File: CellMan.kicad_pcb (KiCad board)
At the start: 2 copper layers, 99.4 x 45 mm, 74 parts, among them J1 Conn_01x04_Male, J2 Conn_01x04_Male, J3 Conn_01x04_Male, J4 Conn_01x02_Female, J5 Conn_01x03_Male, Q1 BSS138W, Q2 STS8DN6LF6AG, Q3 BSS138W, Q4 BSS138W, Q5 BSS138W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

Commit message: something minor
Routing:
- net /SafeGND: track 36.2 -> 62.9 mm, vias 14 -> 17
- net /Balancing: track 3.73 -> 18.0 mm
- net +3V3: track 194.0 -> 192.9 mm

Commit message: zero unrouted traces baby
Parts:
- C4: moved to B.Cu
- moved D4 78.0 mm to (107.5, 118.5), turned to 180 degrees
- moved R21 74.4 mm to (111.3, 118.5), turned to 180 degrees
- moved R19 57.4 mm to (120.7, 117.9), turned to 90 degrees
- moved Q4 56.4 mm to (124.8, 117.8), turned to 180 degrees
- moved C4 13.0 mm to (163.8, 96.7), turned to 180 degrees
- moved C3 9.07 mm to (159.7, 92.9), turned to 270 degrees
- moved U2 5.25 mm to (170.7, 93.1), turned to 180 degrees
- moved C2 1.65 mm to (176.9, 88.0), turned to 90 degrees
- moved U1 0.12 mm to (150.4, 87.9)
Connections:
- ISO2 pad 4: /voltage_measurement/SafeCell- -> /SafeCell-
- U1 pad 16: /Balance_ctl -> Net-(U1-Pad16)
- U1 pad 17: /IO_Sanity_Check -> Net-(U1-Pad17)
- U1 pad 18: +3V3 -> /Balance_ctl
- U1 pad 19: (no net) -> /IO_Sanity_Check
- U1 pad 20: (no net) -> +3V3
- U9 pad 2: /voltage_measurement/SafeCell- -> /SafeCell-
- U9 pad 4: /voltage_measurement/SafeCell- -> /SafeCell-
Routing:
- net /Address_T0: track 2.77 -> 52.8 mm, vias 1 -> 3
- net /Address_T1: track 2.58 -> 52.4 mm, vias 1 -> 3
- net /Address_T2: track 2.25 -> 51.9 mm, vias 1 -> 3
- net /SafeGND: track 62.9 -> 92.0 mm, vias 17 -> 22
- net /Cell+: track 140.5 -> 168.0 mm, vias 2 -> 6
- net +3V3: track 192.9 -> 206.6 mm, vias 13 -> 16
- net /Cell-: track 126.6 -> 138.5 mm, vias 5 -> 3
- net /SCL: track 90.4 -> 98.3 mm, vias 3 -> 4
- net /SDA: track 82.3 -> 88.5 mm, vias 3 -> 4
- net /SafeCell-: track 0.00 -> 5.41 mm, vias 0 -> 3
- net /Balancing: track 18.0 -> 20.8 mm, vias 1 -> 2
- net GND: track 86.2 -> 88.9 mm, vias 4 -> 5
- net /voltage_measurement/SafeCell-: track 2.59 -> 0.00 mm
- net Net-(D4-Pad1): track 0.00 -> 1.84 mm
- net /Balance_ctl: track 32.1 -> 32.2 mm, vias 0 -> 2
- added copper zone on B.Cu, net /SafeCell-

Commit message: memes
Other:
- board text added: "+"
- board text added: "-"
- board text added: "Address Select"
- board text added: "Connor Winiarczyk"
- board text added: "Is this text rules compliant?"
- board text added: "WARNING DO NOT LICK!"
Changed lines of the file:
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@@
   (general
     (thickness 1.6)
-    (drawings 4)
+    (drawings 12)
     (tracks 638)
     (zones 0)
@@
   )
   (setup
-    (last_trace_width 0.25)
+    (last_trace_width 1.5)
     (user_trace_width 1.5)
     (trace_clearance 0.2)
@@
     (tags "resistor handsolder")
     (attr smd)
-    (fp_text reference R19 (at -3.4 0 90) (layer F.SilkS)
+    (fp_text reference R19 (at 3.375 0.025 90) (layer F.SilkS)
       (effects (font (size 1 1) (thickness 0.15)))
     )
@@
     (tags "SOT-323 SC-70 Handsoldering")
     (attr smd)
-    (fp_text reference Q4 (at 0 -2) (layer F.SilkS)
+    (fp_text reference Q4 (at 0 2.375) (layer F.SilkS)
       (effects (font (size 1 1) (thickness 0.15)))
     )
@@
     (descr "Through hole angled pin header, 1x03, 2.54mm pitch, 6mm pin length, single row")
     (tags "Through hole angled pin header THT 1x03 2.54mm single row")
-    (fp_text reference J5 (at 4.385 -2.27) (layer F.SilkS)
+    (fp_text reference J5 (at -2.45 -0.1) (layer F.SilkS)
       (effects (font (size 1 1) (thickness 0.15)))
     )
@@
     (tags "mounting hole 4.5mm")
     (attr virtual)
-    (fp_text reference H7 (at 0 -5.5) (layer F.SilkS)
+    (fp_text reference H7 (at -4.13 -4.96) (layer F.SilkS)
       (effects (font (size 1 1) (thickness 0.15)))
     )
@@
     (tags "mounting hole 4.5mm")
     (attr virtual)
-    (fp_text reference H6 (at 0 -5.5) (layer F.SilkS)
+    (fp_text reference H6 (at -3.575 -4.71) (layer F.SilkS)
       (effects (font (size 1 1) (thickness 0.15)))
     )
@@
     (tags "mounting hole 4.5mm")
     (attr virtual)
-    (fp_text reference H5 (at 0 -5.5) (layer F.SilkS)
+    (fp_text reference H5 (at 3.115 -4.76) (layer F.SilkS)
       (effects (font (size 1 1) (thickness 0.15)))
     )
@@
     (tags "mounting hole 4.5mm")
     (attr virtual)
-    (fp_text reference H4 (at 0 -5.5) (layer F.SilkS)
+    (fp_text reference H4 (at 4.035 -4.15) (layer F.SilkS)
       (effects (font (size 1 1) (thickness 0.15)))
     )
@@
     (tags "mounting hole 4.5mm")
     (attr virtual)
-    (fp_text reference H3 (at 0 -5.5) (layer F.SilkS)
+    (fp_text reference H3 (at 3.185 -4.985) (layer F.SilkS)
       (effects (font (size 1 1) (thickness 0.15)))
     )
@@
     (tags "mounting hole 4.5mm")
     (attr virtual)
-    (fp_text reference H2 (at 0 -5.5) (layer F.SilkS)
+    (fp_text reference H2 (at -2.3 -5.175) (layer F.SilkS)
       (effects (font (size 1 1) (thickness 0.15)))
     )
@@
     (tags "mounting hole 4.5mm")
     (attr virtual)
-    (fp_text reference H1 (at 0 -5.5) (layer F.SilkS)
+    (fp_text reference H1 (at 2.915 -4.9) (layer F.SilkS)
       (effects (font (size 1 1) (thickness 0.15)))
     )
@@
     (descr "8-lead though-hole mounted DIP package, row spacing 7.62 mm (300 mils)")
     (tags "THT DIP DIL PDIP 2.54mm 7.62mm 300mil")
-    (fp_text reference ISO2 (at 3.81 -2.33 90) (layer F.SilkS)
+    (fp_text reference ISO2 (at 3.8753 9.8528 90) (layer F.SilkS)
       (effects (font (size 1 1) (thickness 0.15)))
     )
@@
     (descr "Through hole angled pin header, 1x04, 2.54mm pitch, 6mm pin length, single row")
     (tags "Through hole angled pin header THT 1x04 2.54mm single row")
-    (fp_text reference J1 (at 4.385 -2.27) (layer F.SilkS)
+    (fp_text reference J1 (at -3.45 6.625) (layer F.SilkS)
       (effects (font (size 1 1) (thickness 0.15)))
     )
@@
     (tags "resistor handsolder")
     (attr smd)
-    (fp_text reference R14 (at 0 -1.65 90) (layer F.SilkS)
+    (fp_text reference R14 (at 3.3 0.025 90) (layer F.SilkS)
       (effects (font (size 1 1) (thickness 0.15)))
     )
@@
     )
   )
+  (gr_text "WARNING\nDO NOT LICK!" (at 135.175 107.1) (layer B.SilkS)
+    (effects (font (size 1 1) (thickness 0.15)) (justify mirror))
+  )
+  (gr_text - (at 178.45 105.15 180) (layer F.SilkS)
+    (effects (font (size 4 4) (thickness 0.5)) (justify left))
+  )
+  (gr_text + (at 106.775 107.675 90) (layer F.SilkS)
+    (effects (font (size 4 4) (thickness 0.5)) (justify left))
+  )
+  (gr_text "Address Select" (at 127.85 109.75 90) (layer F.SilkS)
+    (effects (font (size 1 1) (thickness 0.15)) (justify left))
+  )
+  (gr_text "Connor\nWiniarczyk" (at 183.1 120.9) (layer F.Mask)
+    (effects (font (size 1.5 1.5) (thickness 0.3)))
+  )
+  (gr_text "Connor\nWiniarczyk" (at 183.1 120.9) (layer F.Cu)
+    (effects (font (size 1.5 1.5) (thickness 0.3)))
+  )
+  (gr_text "Is this\ntext rules \ncompliant?" (at 117.357143 120.95) (layer B.Mask)
+    (effects (font (size 1.5 1.5) (thickness 0.3)) (justify left mirror))
+  )
+  (gr_text "Is this\ntext rules \ncompliant?" (at 117.357143 120.95) (layer B.Cu)
+    (effects (font (size 1.5 1.5) (thickness 0.3)) (justify left mirror))
+  )
   (gr_line (start 191.08 82.38) (end 191.08 127.38) (layer Edge.Cuts) (width 0.05))
   (gr_line (start 91.66 82.38) (end 191.08 82.38) (layer Edge.Cuts) (width 0.05))
   (gr_line (start 91.66 127.38) (end 191.08 127.38) (layer Edge.Cuts) (width 0.05))
   (gr_line (start 91.66 82.38) (end 91.66 127.38) (layer Edge.Cuts) (width 0.05))
-  (via (at 159.75 94.1) (size 0.8) (drill 0.4) (layers F.Cu B.Cu) (net 3))
-  (via (at 120.7 116.75) (size 0.8) (drill 0.4) (layers F.Cu B.Cu) (net 29))
   (segment (start 109.72 84.23) (end 112.07 84.23) (width 0.25) (layer B.Cu) (net 1))
   (via (at 122.23 84.23) (size 0.8) (drill 0.4) (layers F.Cu B.Cu) (net 1))
@@
   (segment (start 112.92 84.23) (end 118.47 84.23) (width 0.25) (layer B.Cu) (net 1))
   (segment (start 118.47 84.23) (end 119.08 84.23) (width 0.25) (layer B.Cu) (net 1))
-  (via (at 176.93 84.23) (size 0.8) (drill 0.4) (layers F.Cu B.Cu) (net 1))
+  (via (at 176.93 84.23) (size 0.8) (drill 0.4) (layers F.Cu B.Cu) (net 1) (status 1000000))
   (segment (start 176.95 84.25) (end 176.93 84.23) (width 0.25) (layer F.Cu) (net 1))
   (segment (start 176.95 86.925) (end 176.95 84.25) (width 0.25) (layer F.Cu) (net 1))
@@
   (segment (start 134.7 91.85) (end 134.7 93.750002) (width 0.25) (layer B.Cu) (net 2))
   (via (at 134.7 93.750002) (size 0.8) (drill 0.4) (layers F.Cu B.Cu) (net 2))
+  (via (at 159.75 94.1) (size 0.8) (drill 0.4) (layers F.Cu B.Cu) (net 3))
   (via (at 119.6213 106.0831) (size 0.8) (drill 0.4) (layers F.Cu B.Cu) (net 3))
   (via (at 119.5959 107.3023) (size 0.8) (drill 0.4) (layers F.Cu B.Cu) (net 3))
@@
   (segment (start 171.27 117.45) (end 171.27 119.145) (width 0.25) (layer F.Cu) (net 14))
   (segment (start 171.27 119.145) (end 172.025 119.9) (width 0.25) (layer F.Cu) (net 14))
-  (segment (start 135.15 113.25) (end 135.15 112.9) (width 0.25) (layer F.Cu) (net 29))
-  (segment (start 134.2 115.1) (end 134.2 114.2) (width 0.25) (layer F.Cu) (net 29))
-  (segment (start 134.2 114.2) (end 135.15 113.25) (width 0.25) (layer F.Cu) (net 29))
   (segment (start 133.7372 111.5372) (end 133.7372 110.7253) (width 0.25) (layer F.Cu) (net 15))
   (segment (start 134.2 112) (end 133.7372 111.5372) (width 0.25) (layer F.Cu) (net 15))
@@
   (segment (start 161.85 99) (end 161.85 100.72) (width 0.25) (layer F.Cu) (net 28))
   (segment (start 160.15 97.3) (end 161.85 99) (width 0.25) (layer F.Cu) (net 28))
+  (via (at 120.7 116.75) (size 0.8) (drill 0.4) (layers F.Cu B.Cu) (net 29))
+  (segment (start 135.15 113.25) (end 135.15 112.9) (width 0.25) (layer F.Cu) (net 29))
+  (segment (start 134.2 115.1) (end 134.2 114.2) (width 0.25) (layer F.Cu) (net 29))
+  (segment (start 134.2 114.2) (end 135.15 113.25) (width 0.25) (layer F.Cu) (net 29))
   (via (at 134.97 111.77) (size 0.8) (drill 0.4) (layers F.Cu B.Cu) (net 29))
   (segment (start 135.15 112.9) (end 135.15 111.95) (width 0.25) (layer F.Cu) (net 29))

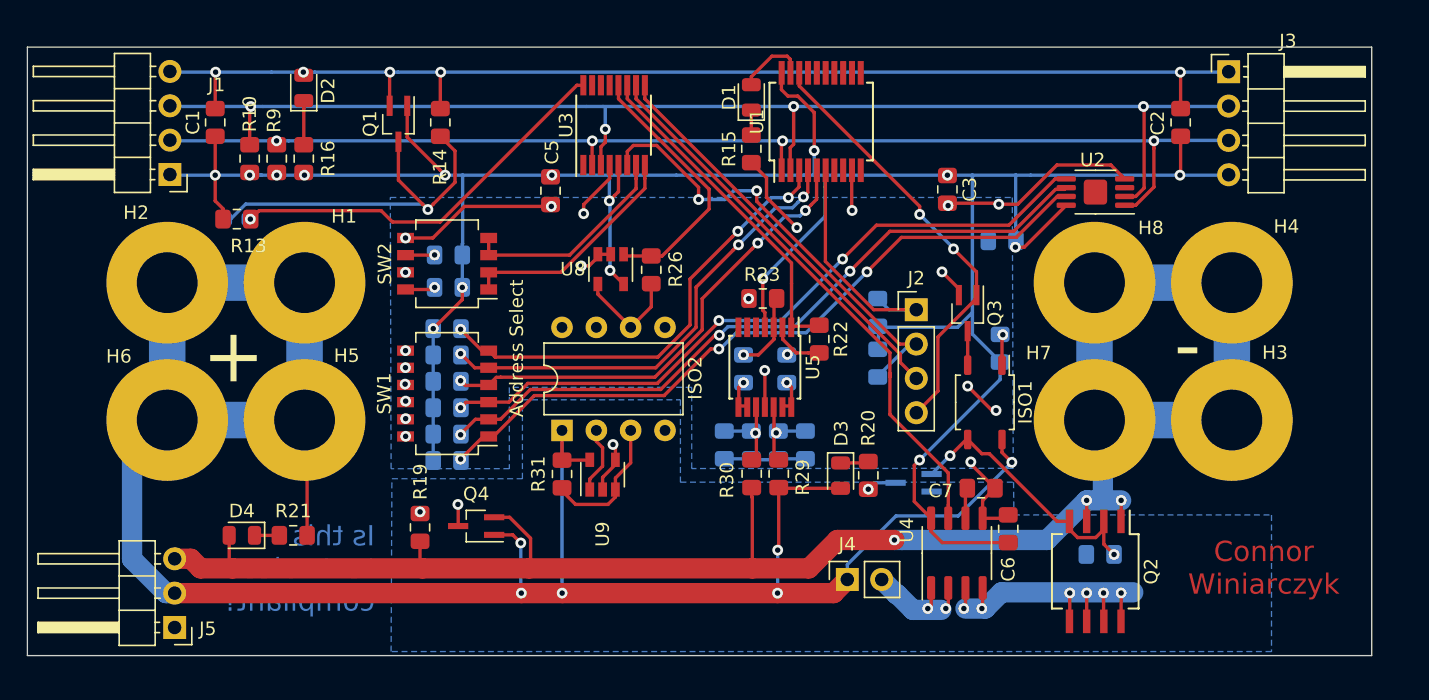
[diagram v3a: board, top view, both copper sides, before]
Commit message: Reviewed board, 10 unrouted traces to go
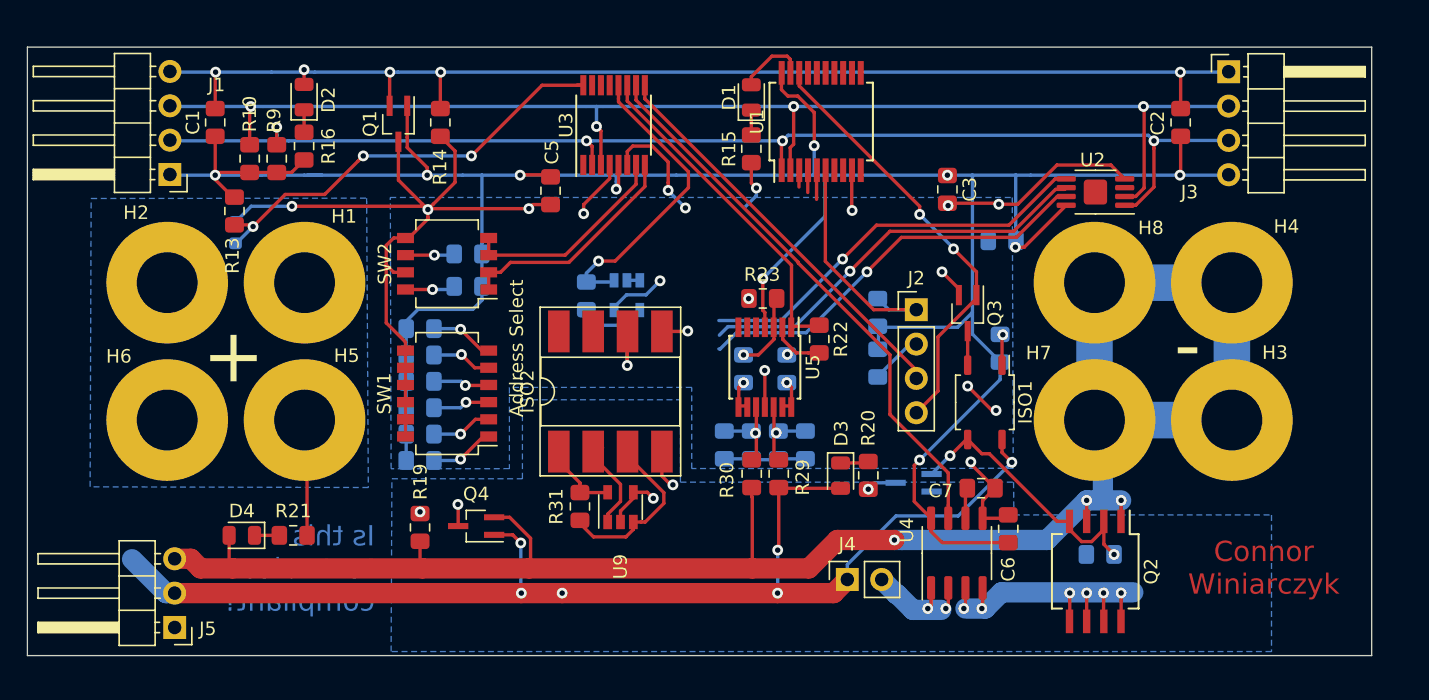
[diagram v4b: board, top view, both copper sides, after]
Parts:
- ISO2: footprint Package_DIP:DIP-8_W7.62mm -> Package_DIP:DIP-8_W8.89mm_SMDSocket_LongPads
- R26, U8: moved to B.Cu
- moved R26 5.17 mm to (133.0, 100.8)
- moved ISO2 4.59 mm to (134.8, 107.8)
- moved U9 2.74 mm to (135.5, 116.4)
- moved R31 2.74 mm to (132.5, 116.3)
- moved U8 2.27 mm to (136.0, 100.7)
- moved R1 2.00 mm to (120.7, 113.0)
- moved R2 2.00 mm to (120.7, 111.0)
- moved R3 2.00 mm to (120.7, 109.0)
- moved R4 2.00 mm to (120.7, 107.1)
- moved R5 2.00 mm to (120.7, 105.2)
- moved R6 2.00 mm to (120.7, 103.2)
- moved R11 1.45 mm to (124.2, 100.1)
- moved R12 1.45 mm to (124.2, 97.7)
- moved TH1 1.00 mm to (107.0, 96.1), turned to 90 degrees
- moved R16 0.93 mm to (112.1, 89.7)
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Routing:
- net /Cell+: track 168.0 -> 109.2 mm
- net /Address_G0: track 35.6 -> 6.23 mm, vias 3 -> 1
- net /Address_G1: track 34.8 -> 6.09 mm, vias 3 -> 1
- net /Address_G2: track 34.2 -> 5.85 mm, vias 3 -> 1
- net /~ADC_INT: track 33.9 -> 12.4 mm
- net /Address_T1: track 52.4 -> 34.7 mm, vias 3 -> 2
- net /Address_T2: track 51.9 -> 34.2 mm, vias 3 -> 2
- net /Address_T0: track 52.8 -> 35.5 mm, vias 3 -> 2
- net /SafeGND: track 92.0 -> 108.2 mm, vias 22 -> 15
- net +3V3: track 206.6 -> 215.0 mm, vias 16 -> 11
- net /SafeCell-: track 5.41 -> 9.64 mm, vias 3 -> 4
- net /Temperature: track 29.4 -> 32.6 mm, vias 1 -> 3
- net Net-(ISO2-Pad3): track 10.2 -> 13.1 mm
- net /CellVoltage_01: track 19.7 -> 22.6 mm, vias 0 -> 1
- net /SDA: track 88.5 -> 91.3 mm
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- added copper zone on B.Cu, net /Cell+
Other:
- net class Default: clearance 0.2 -> 0.254
- rule trace_clearance: 0.2 -> 0.254

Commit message: Fixed some problems
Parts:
- moved C3 3.97 mm to (163.4, 91.4)
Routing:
- net /Cell-: track 138.5 -> 98.4 mm
- net /Address_G0: track 6.23 -> 39.9 mm, vias 1 -> 3
- net /Address_G1: track 6.09 -> 38.4 mm, vias 1 -> 3
- net /Address_G2: track 5.85 -> 37.5 mm, vias 1 -> 3
- net /~ADC_INT: track 12.4 -> 34.1 mm
- net /Address_T0: track 35.5 -> 55.9 mm, vias 2 -> 3
- net /Cell+: track 109.2 -> 129.3 mm, vias 6 -> 7
- net /Address_T1: track 34.7 -> 54.3 mm, vias 2 -> 3
- net /Address_T2: track 34.2 -> 53.8 mm, vias 2 -> 3
- net +3V3: track 215.0 -> 230.1 mm
- net /SafeGND: track 108.2 -> 116.9 mm
- net /Balance_ctl: track 32.2 -> 37.6 mm
- net Net-(ISO1-Pad1): track 2.27 -> 5.33 mm
- net Net-(Q5-Pad3): track 2.22 -> 3.34 mm
- net /CellVoltage_01: track 22.6 -> 21.8 mm
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- added copper zone on B.Cu, net /Cell-
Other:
- rule trace_min: 0.2 -> 0
- board text added: "CellMan"
- board text removed: "Connor Winiarczyk"

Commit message: mounting
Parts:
- removed H1, H5, H7, H8: MountingHole_Pad, MountingHole:MountingHole_4.5mm_Pad
- removed Q3: BSS138W, Package_TO_SOT_SMD:SOT-323_SC-70_Handsoldering
- added JP1: Jumper, Connector_PinSocket_2.54mm:PinSocket_1x02_P2.54mm_Vertical, F.Cu at (141.1, 115.7)
- added JP2: SolderJumper_2_Open, Jumper:SolderJumper-2_P1.3mm_Open_RoundedPad1.0x1.5mm, B.Cu at (144.1, 115.5)
- added R32: 61, Resistor_SMD:R_0805_2012Metric_Pad1.15x1.40mm_HandSolder, B.Cu at (144.1, 119.0)
- C4, R17: moved to F.Cu
- C5: value C -> 1uF
- H2, H3, H4, H6: footprint MountingHole:MountingHole_4.5mm_Pad -> MountingHole:MountingHole_4mm_Pad
- R1, R10, R11, R12, R2, R3, R4, R5, R6, R7, R8, R9: value R -> 5k
- R16: value 0 -> R
- U2: footprint Package_SO:MSOP-8-1EP_3x3mm_P0.65mm_EP1.73x1.85mm -> Package_SO:MSOP-8_3x3mm_P0.65mm
- moved TH1 5.63 mm to (112.4, 97.8)
- moved C4 5.39 mm to (168.0, 93.3), turned to 0 degrees
- moved R13 4.51 mm to (110.3, 97.6)
- moved U2 4.51 mm to (169.7, 97.5)
- moved R17 1.47 mm to (162.7, 103.5), turned to 180 degrees
- moved H4 1.23 mm to (179.5, 100.0)
- moved H3 1.22 mm to (179.5, 110.0)
- moved R18 0.95 mm to (170.2, 119.4)
- moved ISO2 0.57 mm to (134.7, 107.3)
- moved Q4 0.51 mm to (124.3, 117.9)
- moved H2 0.43 mm to (102.4, 100.0)
- moved H6 0.39 mm to (102.4, 110.0)
- moved R15 0.30 mm to (145.2, 90.2), turned to 270 degrees
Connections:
- C1 pad 1: +3V3 -> +5V
- C2 pad 1: +3V3 -> +5V
- C3 pad 1: +3V3 -> +5V
- C4 pad 1: +3V3 -> +5V
- C5 pad 1: +3V3 -> +5V
- C6 pad 1: +3V3 -> +5V
- ISO1 pad 2: Net-(ISO1-Pad2) -> /SafeGND
- ISO2 pad 1: /Cell+ -> Net-(ISO2-Pad1)
- ISO2 pad 2: Net-(ISO2-Pad2) -> /SafeCell-
- J1 pad 1: +3V3 -> +5V
- J3 pad 4: +3V3 -> +5V
- Q1 pad 1: +3V3 -> +5V
- R1 pad 1: +3V3 -> +5V
- R10 pad 1: +3V3 -> +5V
- R11 pad 1: +3V3 -> +5V
- R12 pad 1: +3V3 -> +5V
- R13 pad 2: +3V3 -> +5V
- R15 pad 1: /SafeGND -> Net-(D1-Pad1)
- R15 pad 2: Net-(D1-Pad1) -> /SafeGND
- R16 pad 1: +3V3 -> +5V
- R17 pad 1: +3V3 -> Net-(ISO1-Pad1)
- R17 pad 2: Net-(ISO1-Pad1) -> /Balance_ctl
- R2 pad 1: +3V3 -> +5V
- R29 pad 1: /Cell+ -> Net-(JP1-Pad1)
- R3 pad 1: +3V3 -> +5V
- R31 pad 1: /Cell+ -> Net-(JP1-Pad1)
- R4 pad 1: +3V3 -> +5V
- R5 pad 1: +3V3 -> +5V
- R6 pad 1: +3V3 -> +5V
- R7 pad 1: +3V3 -> +5V
- R8 pad 1: +3V3 -> +5V
- R9 pad 1: +3V3 -> +5V
- U1 pad 20: +3V3 -> +5V
- U2 pad 8: +3V3 -> +5V
- U3 pad 5: +3V3 -> +5V
- U4 pad 8: +3V3 -> +5V
- U5 pad 4: +3V3 -> +5V
- U5 pad 5: Net-(U5-Pad5) -> Net-(R23-Pad2)
- U5 pad 7: Net-(U5-Pad7) -> Net-(U5-Pad6)
- U8 pad 5: +3V3 -> +5V
- U9 pad 1: Net-(ISO2-Pad2) -> Net-(ISO2-Pad1)
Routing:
- net +3V3: track 230.1 -> 0.00 mm, vias 11 -> 0
- net +5V: track 0.00 -> 230.0 mm, vias 0 -> 14
- net Net-(JP1-Pad1): track 0.00 -> 23.2 mm, vias 0 -> 2
- net /Cell+: track 129.3 -> 116.8 mm, vias 7 -> 6
- net Net-(ISO2-Pad1): track 0.00 -> 10.1 mm
- net /SafeCell-: track 9.64 -> 18.2 mm
- net /SafeGND: track 116.9 -> 108.5 mm, vias 15 -> 13
- net Net-(ISO2-Pad2): track 7.09 -> 0.00 mm
- net /SDA: track 91.3 -> 96.7 mm
- net /SCL: track 98.0 -> 103.3 mm
- net /Cell-: track 98.4 -> 93.4 mm, vias 3 -> 7
- net Net-(JP1-Pad2): track 0.00 -> 4.91 mm
- net Net-(ISO1-Pad1): track 5.33 -> 2.40 mm, vias 1 -> 0
- net /Temperature: track 32.6 -> 35.0 mm
- net Net-(ISO1-Pad2): track 2.35 -> 0.00 mm
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- added copper zone on F.Cu, net (none)
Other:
- board text added: "CellMan v0.7"
- board text added: "Connor Winiarczyk"
- board text added: "Made in The USA"
- board text added: "https://github.com/Lafayette-FSAE/CellMan"
- board text removed: "CellMan"
- board text removed: "Is this text rules compliant?"
